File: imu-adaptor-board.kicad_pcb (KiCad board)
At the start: 2 copper layers, 49.5 x 48.3 mm, 7 parts, among them M3_MOUNT VAL**, P1 IMU-CAN, P2 IMU-SPI3, U1 ADIS16405BMLZ

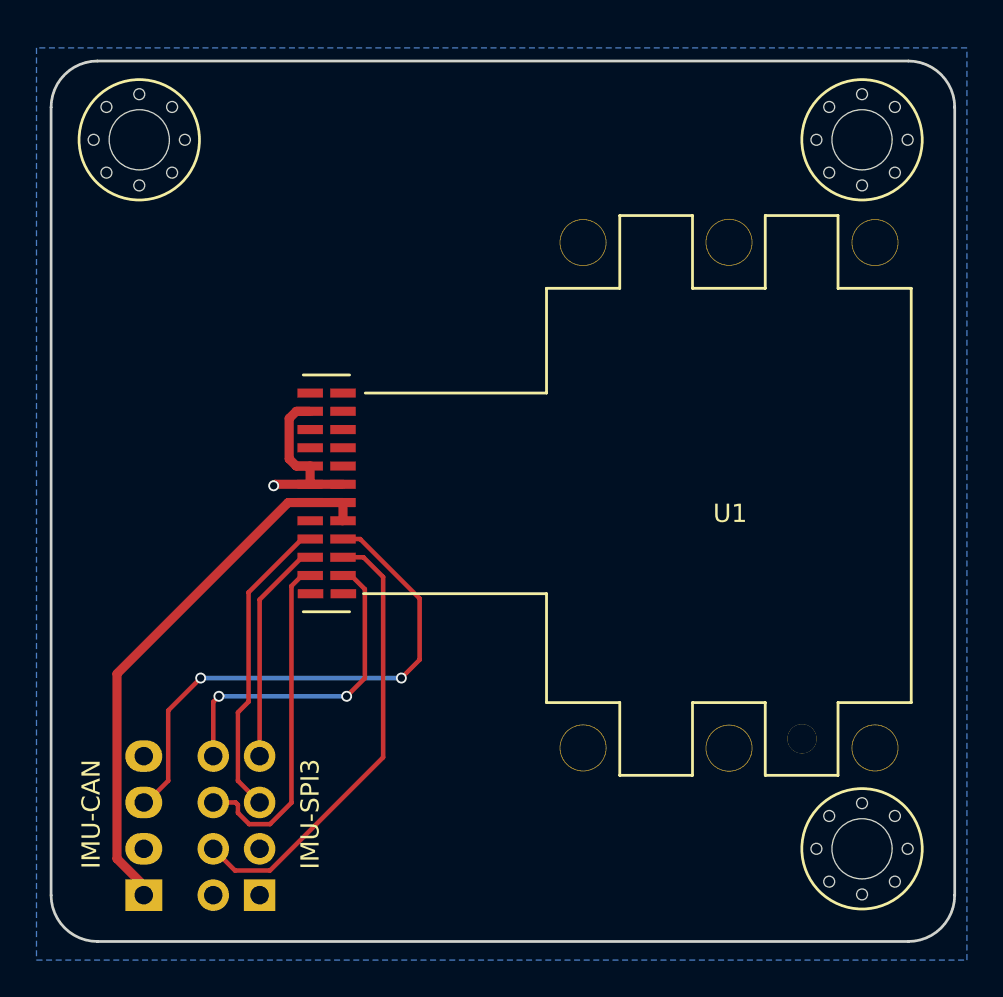
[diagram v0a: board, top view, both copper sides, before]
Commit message: Add ADIS16405 origin and make board square
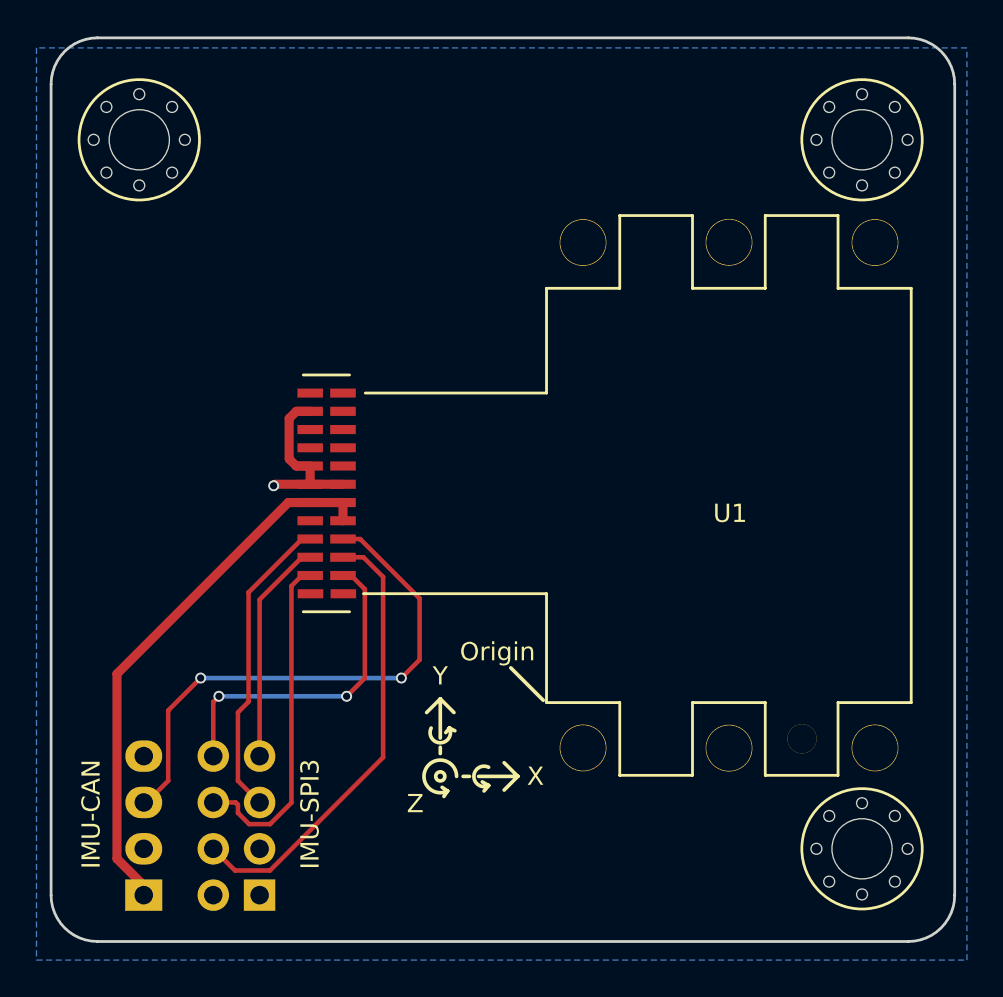
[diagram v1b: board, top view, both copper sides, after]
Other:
- board size 49.5 x 48.3 mm -> 49.5 x 49.5 mm
- net class Default: clearance 0.2 -> 0.19; trace_width 0.25 -> 0.28; via_dia 0.6 -> 0.8
- net class POWER removed
- net class Power added: clearance 0.19, trace_width 0.5, via_dia 0.8, via_drill 0.4
- rule pad_to_mask_clearance: 0.2 -> 0
- rule trace_clearance: 0.2 -> 0.19
- rule trace_min: 0.2 -> 0.19
- board text added: "Origin"
- board text added: "X"
- board text added: "Y"
- board text added: "Z"
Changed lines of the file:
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@@
 (kicad_pcb (version 4) (host pcbnew 4.0.2-4+6225~38~ubuntu15.10.1-stable)
   (general
-    (links 0)
+    (links 15)
     (no_connects 0)
     (area 50.724999 45.644999 100.405001 94.055001)
     (thickness 1.6)
-    (drawings 10)
+    (drawings 35)
     (tracks 62)
     (zones 0)
@@
   )
   (setup
-    (last_trace_width 0.25)
-    (trace_clearance 0.2)
+    (last_trace_width 0.28)
+    (user_trace_width 0.2)
+    (user_trace_width 0.3)
+    (user_trace_width 0.5)
+    (user_trace_width 0.8)
+    (user_trace_width 1)
+    (user_trace_width 1.5)
+    (user_trace_width 2)
+    (user_trace_width 3)
+    (trace_clearance 0.19)
     (zone_clearance 0.508)
     (zone_45_only no)
-    (trace_min 0.2)
+    (trace_min 0.19)
     (segment_width 0.2)
-    (edge_width 0.15)
-    (via_size 0.6)
+    (edge_width 0.1)
+    (via_size 0.8)
     (via_drill 0.4)
     (via_min_size 0.4)
     (via_min_drill 0.3)
-    (uvia_size 0.3)
-    (uvia_drill 0.1)
+    (uvia_size 0.8)
+    (uvia_drill 0.4)
     (uvias_allowed no)
     (uvia_min_size 0.2)
@@
     (mod_text_size 1 1)
     (mod_text_width 0.15)
-    (pad_size 1.524 1.524)
-    (pad_drill 0.762)
-    (pad_to_mask_clearance 0.2)
+    (pad_size 3.3 3.3)
+    (pad_drill 3.3)
+    (pad_to_mask_clearance 0)
     (aux_axis_origin 0 0)
-    (visible_elements FFFFFF7F)
+    (grid_origin 215.519 117.983)
+    (visible_elements 7FFFFFFF)
     (pcbplotparams
-      (layerselection 0x00030_80000001)
+      (layerselection 0x00008_7ffffffe)
       (usegerberextensions false)
       (excludeedgelayer true)
@@
       (padsonsilk false)
       (subtractmaskfromsilk false)
-      (outputformat 1)
+      (outputformat 3)
       (mirror false)
-      (drillshape 1)
+      (drillshape 0)
       (scaleselection 1)
-      (outputdirectory ""))
+      (outputdirectory Gerbers/))
   )
   (net 0 "")
@@
   (net 21 "Net-(U1-Pad24)")
   (net_class Default "This is the default net class."
-    (clearance 0.2)
-    (trace_width 0.25)
-    (via_dia 0.6)
+    (clearance 0.19)
+    (trace_width 0.28)
+    (via_dia 0.8)
     (via_drill 0.4)
-    (uvia_dia 0.3)
-    (uvia_drill 0.1)
+    (uvia_dia 0.8)
+    (uvia_drill 0.4)
     (add_net /CAN1_RX)
     (add_net /CAN1_TX)
@@
     (add_net "Net-(U1-Pad9)")
   )
-  (net_class POWER ""
-    (clearance 0.2)
+  (net_class Power ""
+    (clearance 0.19)
     (trace_width 0.5)
-    (via_dia 0.6)
+    (via_dia 0.8)
     (via_drill 0.4)
-    (uvia_dia 0.3)
-    (uvia_drill 0.1)
+    (uvia_dia 0.8)
+    (uvia_drill 0.4)
     (add_net +3V3)
     (add_net +5V)
@@
       (xy 1.476375 1.335759) (xy 1.476375 1.335759)) (layer B.SilkS) (width 0.1))
   )
+  (dimension 49.53 (width 0.3) (layer Dwgs.User)
+    (gr_text "49.530 mm" (at 75.565 99.14) (layer Dwgs.User)
+      (effects (font (size 1.5 1.5) (thickness 0.3)))
+    )
+    (feature1 (pts (xy 100.33 93.98) (xy 100.33 100.49)))
+    (feature2 (pts (xy 50.8 93.98) (xy 50.8 100.49)))
+    (crossbar (pts (xy 50.8 97.79) (xy 100.33 97.79)))
+    (arrow1a (pts (xy 100.33 97.79) (xy 99.203496 98.376421)))
+    (arrow1b (pts (xy 100.33 97.79) (xy 99.203496 97.203579)))
+    (arrow2a (pts (xy 50.8 97.79) (xy 51.926504 98.376421)))
+    (arrow2b (pts (xy 50.8 97.79) (xy 51.926504 97.203579)))
+  )
+  (dimension 49.53 (width 0.3) (layer Dwgs.User)
+    (gr_text "49.530 mm" (at 45.64 69.215 270) (layer Dwgs.User)
+      (effects (font (size 1.5 1.5) (thickness 0.3)))
+    )
+    (feature1 (pts (xy 50.8 93.98) (xy 44.29 93.98)))
+    (feature2 (pts (xy 50.8 44.45) (xy 44.29 44.45)))
+    (crossbar (pts (xy 46.99 44.45) (xy 46.99 93.98)))
+    (arrow1a (pts (xy 46.99 93.98) (xy 46.403579 92.853496)))
+    (arrow1b (pts (xy 46.99 93.98) (xy 47.576421 92.853496)))
+    (arrow2a (pts (xy 46.99 44.45) (xy 46.403579 45.576504)))
+    (arrow2b (pts (xy 46.99 44.45) (xy 47.576421 45.576504)))
+  )
   (gr_text "R. Wareham\nR. Taylor-Davies" (at 77 89) (layer B.SilkS)
     (effects (font (size 1.5 1.5) (thickness 0.3)) (justify mirror))
@@
   )
   (gr_arc (start 53.34 91.44) (end 53.34 93.98) (angle 90) (layer Edge.Cuts) (width 0.15))
-  (gr_arc (start 53.34 48.26) (end 50.8 48.26) (angle 90) (layer Edge.Cuts) (width 0.15))
-  (gr_arc (start 97.79 48.26) (end 97.79 45.72) (angle 90) (layer Edge.Cuts) (width 0.15))
+  (gr_arc (start 53.34 46.99) (end 50.8 46.99) (angle 90) (layer Edge.Cuts) (width 0.15))
+  (gr_arc (start 97.79 46.99) (end 97.79 44.45) (angle 90) (layer Edge.Cuts) (width 0.15))
   (gr_arc (start 97.79 91.44) (end 100.33 91.44) (angle 90) (layer Edge.Cuts) (width 0.15))
   (gr_line (start 97.79 93.98) (end 53.34 93.98) (layer Edge.Cuts) (width 0.15))
-  (gr_line (start 100.33 48.26) (end 100.33 91.44) (layer Edge.Cuts) (width 0.15))
-  (gr_line (start 53.34 45.72) (end 97.79 45.72) (layer Edge.Cuts) (width 0.15))
-  (gr_line (start 50.8 91.44) (end 50.8 48.26) (layer Edge.Cuts) (width 0.15))
+  (gr_line (start 100.33 46.99) (end 100.33 91.44) (layer Edge.Cuts) (width 0.15))
+  (gr_line (start 53.34 44.45) (end 97.79 44.45) (layer Edge.Cuts) (width 0.15))
+  (gr_line (start 50.8 91.44) (end 50.8 46.99) (layer Edge.Cuts) (width 0.15))
+  (gr_line (start 77.7765 80.75909) (end 75.9985 78.98109) (angle 90) (layer F.SilkS) (width 0.2))
+  (gr_text Origin (at 77.343 78.105) (layer F.SilkS)
+    (effects (font (size 1 1) (thickness 0.15)) (justify right))
+  )
+  (gr_line (start 72.533 85.73059) (end 72.333 86.03059) (layer F.SilkS) (width 0.2))
+  (gr_line (start 72.533 85.73059) (end 72.233 85.53059) (layer F.SilkS) (width 0.2))
+  (gr_arc (start 72.133 84.93059) (end 72.533 85.73059) (angle 296.5650512) (layer F.SilkS) (width 0.2))
+  (gr_line (start 72.133 83.68059) (end 72.133 83.33059) (layer F.SilkS) (width 0.2))
+  (gr_line (start 72.633 82.28059) (end 72.933 82.43059) (layer F.SilkS) (width 0.2))
+  (gr_line (start 72.433 82.53059) (end 72.633 82.28059) (layer F.SilkS) (width 0.2))
+  (gr_line (start 72.133 82.83059) (end 72.133 80.68059) (layer F.SilkS) (width 0.2))
+  (gr_arc (start 72.133 82.53059) (end 72.633 82.28059) (angle 233.1301024) (layer F.SilkS) (width 0.2))
+  (gr_line (start 72.133 80.68059) (end 72.883 81.43059) (layer F.SilkS) (width 0.2))
+  (gr_line (start 72.133 80.68059) (end 71.383 81.43059) (layer F.SilkS) (width 0.2))
+  (gr_line (start 74.783 85.43059) (end 74.533 85.73059) (layer F.SilkS) (width 0.2))
+  (gr_line (start 74.433 85.23059) (end 74.783 85.43059) (layer F.SilkS) (width 0.2))
+  (gr_line (start 74.233 84.93059) (end 76.383 84.93059) (layer F.SilkS) (width 0.2))
+  (gr_arc (start 74.533 84.93059) (end 74.783 85.43059) (angle 233.1301024) (layer F.SilkS) (width 0.2))
+  (gr_text Y (at 72.133 79.43059) (layer F.SilkS)
+    (effects (font (size 1 1) (thickness 0.25)))
+  )
+  (gr_text X (at 76.883 84.93059) (layer F.SilkS)
+    (effects (font (size 1 1) (thickness 0.25)) (justify left))
+  )
+  (gr_text Z (at 71.233 86.43059) (layer F.SilkS)
+    (effects (font (size 1 1) (thickness 0.25)) (justify right))
+  )
+  (gr_line (start 76.383 84.93059) (end 75.633 85.68059) (layer F.SilkS) (width 0.2))
+  (gr_line (start 76.383 84.93059) (end 75.633 84.18059) (layer F.SilkS) (width 0.2))
+  (gr_line (start 73.383 84.93059) (end 73.733 84.93059) (layer F.SilkS) (width 0.2))
+  (gr_circle (center 72.133 84.93059) (end 72.133 85.18059) (layer F.SilkS) (width 0.2))
   (segment (start 66.799998 69.919988) (end 66.799998 70.909786) (width 0.5) (layer F.Cu) (net 1) (status 30))
   (segment (start 66.799998 70.909786) (end 66.789798 70.919986) (width 0.5) (layer F.Cu) (net 1) (status 30))
@@
   (via (at 59 79.54) (size 0.6) (drill 0.4) (layers F.Cu B.Cu) (net 3))
   (segment (start 57.22101 81.31899) (end 59 79.54) (width 0.25) (layer F.Cu) (net 3))
-  (segment (start 65 68.91999) (end 63.08001 68.91999) (width 0.5) (layer F.Cu) (net 4))
+  (segment (start 65 68.91999) (end 63.08001 68.91999) (width 0.5) (layer F.Cu) (net 4) (status 10))
   (segment (start 63.08001 68.91999) (end 63 69) (width 0.5) (layer F.Cu) (net 4))
   (via (at 63 69) (size 0.6) (drill 0.4) (layers F.Cu B.Cu) (net 4))
-  (segment (start 65 68.91999) (end 66.799998 68.91999) (width 0.5) (layer F.Cu) (net 4))
-  (segment (start 65 67.919992) (end 65 68.91999) (width 0.5) (layer F.Cu) (net 4))
-  (segment (start 65 64.919998) (end 64.239996 64.919998) (width 0.5) (layer F.Cu) (net 4))
+  (segment (start 65 68.91999) (end 66.799998 68.91999) (width 0.5) (layer F.Cu) (net 4) (status 30))
+  (segment (start 65 67.919992) (end 65 68.91999) (width 0.5) (layer F.Cu) (net 4) (status 30))
+  (segment (start 65 64.919998) (end 64.239996 64.919998) (width 0.5) (layer F.Cu) (net 4) (status 10))
   (segment (start 64.239996 64.919998) (end 63.849999 65.309995) (width 0.5) (layer F.Cu) (net 4))
   (segment (start 63.849999 65.309995) (end 63.849999 67.529995) (width 0.5) (layer F.Cu) (net 4))
   (segment (start 63.849999 67.529995) (end 64.239996 67.919992) (width 0.5) (layer F.Cu) (net 4))
-  (segment (start 64.239996 67.919992) (end 65 67.919992) (width 0.5) (layer F.Cu) (net 4))
+  (segment (start 64.239996 67.919992) (end 65 67.919992) (width 0.5) (layer F.Cu) (net 4) (status 20))
   (segment (start 69 83.88913) (end 69 74) (width 0.25) (layer F.Cu) (net 6))
   (segment (start 69 74) (end 67.919982 72.919982) (width 0.25) (layer F.Cu) (net 6))
